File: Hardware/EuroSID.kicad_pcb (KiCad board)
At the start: 2 copper layers, 213.3 x 106.6 mm, 77 parts, among them U1 TLC5947DAP, U10 LM1117-5.0, U11 L7809, U12 STM32F030R8Tx, U13 LM1117-3.3, U2 MCP6002-xSN, U3 MCP6004, U4 OPA1678, U5 MCP6002-xSN, U6 74HC595, U7 74HC595, U8 SID, U9 LM1117-3.3

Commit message: Fixed issues with footprints
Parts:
- added D28: LM4040DBZ-10, Package_TO_SOT_SMD:SOT-23, F.Cu at (197.0, 56.0)
- added J16: Conn_ARM_JTAG_SWD_10, Connector_PinHeader_1.27mm:PinHeader_2x05_P1.27mm_Vertical_SMD, F.Cu at (199.6, 46.9)
- added Q1: MMBT3904, Package_TO_SOT_SMD:SOT-23, F.Cu at (169.4, 61.8)
- added Q2: MMBT3904, Package_TO_SOT_SMD:SOT-23, F.Cu at (172.8, 61.8)
- added Q3: MMBT3904, Package_TO_SOT_SMD:SOT-23, F.Cu at (176.3, 61.8)
- added X1: ACO-xxxMHz, Oscillator:Oscillator_DIP-14, F.Cu at (170.6, 53.6)
- C1, C10, C11, C12, C13, C14, C15, C16, C17, C18, C19, C2, C20, C21, C22, C23, C24, C25, C26, C27, C28, C3, C31, C39, C4, C40, C41, C44, C45, C48, C49, C5, C50, C51, C53, C54, C55, C56, C57, C6, C61, C62, C63, C7, C8, C9: footprint Capacitors_SMD:C_0603 -> Capacitor_SMD:C_0603_1608Metric
- moved C31 298.4 mm to (133.5, 56.2)
- moved C41 298.4 mm to (133.5, 80.0)
- moved U10 298.4 mm to (116.8, 72.6)
- moved U11 298.4 mm to (118.9, 58.9)
- moved C1 281.2 mm to (87.3, 60.3)
- moved C2 281.2 mm to (84.4, 58.9)
- moved C3 281.2 mm to (87.3, 58.9)
- moved C30 281.2 mm to (68.6, 74.1)
- moved C32 281.2 mm to (53.3, 52.0)
- moved C4 281.2 mm to (84.4, 60.3)
- moved C45 281.2 mm to (84.4, 61.6)
- moved C49 281.2 mm to (94.5, 51.6)
- moved C51 281.2 mm to (94.5, 50.3)
- moved C52 281.2 mm to (96.9, 42.0)
- moved C53 281.2 mm to (91.7, 53.9)
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
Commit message: Added PJ398SM model
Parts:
- added C65: 100 nF, Capacitor_SMD:C_0603_1608Metric, F.Cu at (165.0, 100.4)
- added C66: 100 nF, Capacitor_SMD:C_0603_1608Metric, F.Cu at (212.2, 70.6)
- added C67: 100 nF, Capacitor_SMD:C_0603_1608Metric, F.Cu at (202.2, 87.0)
- added C68: 100 nF, Capacitor_SMD:C_0603_1608Metric, F.Cu at (199.2, 90.0)
- added J1: GATE_2, Connector_Audio:Jack_3.5mm_QingPu_WQP-PJ398SM_Vertical_CircularHoles, F.Cu at (242.0, 71.5)
- added J10: IN_2, Connector_Audio:Jack_3.5mm_QingPu_WQP-PJ398SM_Vertical_CircularHoles, F.Cu at (172.6, 86.3)
- added J11: IN_3, Connector_Audio:Jack_3.5mm_QingPu_WQP-PJ398SM_Vertical_CircularHoles, F.Cu at (182.6, 71.5)
- added J12: PWM_CV, Connector_Audio:Jack_3.5mm_QingPu_WQP-PJ398SM_Vertical_CircularHoles, F.Cu at (172.6, 71.5)
- added J2: GATE_3, Connector_Audio:Jack_3.5mm_QingPu_WQP-PJ398SM_Vertical_CircularHoles, F.Cu at (231.9, 71.5)
- added J3: GATE_1, Connector_Audio:Jack_3.5mm_QingPu_WQP-PJ398SM_Vertical_CircularHoles, F.Cu at (221.0, 67.3)
- added J4: OUT2_CON, Connector_Audio:Jack_3.5mm_QingPu_WQP-PJ398SM_Vertical_CircularHoles, F.Cu at (162.5, 86.3)
- added J5: EXT_CON, Connector_Audio:Jack_3.5mm_QingPu_WQP-PJ398SM_Vertical_CircularHoles, F.Cu at (162.5, 71.5)
- added J6: CUTOFF_CV, Connector_Audio:Jack_3.5mm_QingPu_WQP-PJ398SM_Vertical_CircularHoles, F.Cu at (192.7, 86.3)
- added J7: SHAPE_CV, Connector_Audio:Jack_3.5mm_QingPu_WQP-PJ398SM_Vertical_CircularHoles, F.Cu at (202.7, 71.5)
- added J8: OUT1_CON, Connector_Audio:Jack_3.5mm_QingPu_WQP-PJ398SM_Vertical_CircularHoles, F.Cu at (192.7, 71.5)
- added J9: IN_1, Connector_Audio:Jack_3.5mm_QingPu_WQP-PJ398SM_Vertical_CircularHoles, F.Cu at (182.6, 86.3)
- added R1: 1640, Resistor_SMD:R_0603_1608Metric, F.Cu at (224.4, 85.5)
- added R10: 100k, Resistor_SMD:R_0603_1608Metric, F.Cu at (248.5, 75.1)
- added R11: 10k, Resistor_SMD:R_0603_1608Metric, F.Cu at (239.4, 85.5)
- added R12: 10k, Resistor_SMD:R_0603_1608Metric, F.Cu at (236.4, 87.0)
- added R13: 10k, Resistor_SMD:R_0603_1608Metric, F.Cu at (248.5, 73.6)
- added R14: 10k, Resistor_SMD:R_0603_1608Metric, F.Cu at (233.4, 87.0)
- added R15: 10k, Resistor_SMD:R_0603_1608Metric, F.Cu at (236.4, 85.5)
- added R16: 10k, Resistor_SMD:R_0603_1608Metric, F.Cu at (233.4, 85.5)
- added R17: 10k, Resistor_SMD:R_0603_1608Metric, F.Cu at (230.4, 87.0)
- added R18: 10k, Resistor_SMD:R_0603_1608Metric, F.Cu at (248.5, 78.2)
- added R19: 10k, Resistor_SMD:R_0603_1608Metric, F.Cu at (218.4, 85.5)
- added R2: 10k, Resistor_SMD:R_0603_1608Metric, F.Cu at (218.4, 87.0)
- added R20: 10k, Resistor_SMD:R_0603_1608Metric, F.Cu at (230.4, 85.5)
- added R21: 10k, Resistor_SMD:R_0603_1608Metric, F.Cu at (248.5, 72.1)
- added R22: 10k, Resistor_SMD:R_0603_1608Metric, F.Cu at (227.4, 85.5)
- added R23: 10k, Resistor_SMD:R_0603_1608Metric, F.Cu at (224.4, 87.0)
- added R24: 10k, Resistor_SMD:R_0603_1608Metric, F.Cu at (168.0, 100.4)
- added R25: 30k, Resistor_SMD:R_0603_1608Metric, F.Cu at (171.0, 100.4)
- added R26: 1k, Resistor_SMD:R_0603_1608Metric, F.Cu at (174.0, 100.4)
- added R27: 50k, Resistor_SMD:R_0603_1608Metric, F.Cu at (199.2, 85.5)
- added R28: 10k, Resistor_SMD:R_0603_1608Metric, F.Cu at (177.0, 100.4)
- added R29: 30k, Resistor_SMD:R_0603_1608Metric, F.Cu at (209.2, 70.6)
- added R3: 10k, Resistor_SMD:R_0603_1608Metric, F.Cu at (221.4, 85.5)
- added R30: 120k, Resistor_SMD:R_0603_1608Metric, F.Cu at (180.1, 100.4)
- added R31: 100k, Resistor_SMD:R_0603_1608Metric, F.Cu at (162.0, 100.4)
- added R32: 120k, Resistor_SMD:R_0603_1608Metric, F.Cu at (159.0, 100.4)
- added R33: 100k, Resistor_SMD:R_0603_1608Metric, F.Cu at (209.2, 72.1)
- added R34: 120k, Resistor_SMD:R_0603_1608Metric, F.Cu at (202.2, 85.5)
- added R35: 120k, Resistor_SMD:R_0603_1608Metric, F.Cu at (212.2, 72.1)
- added R36: 1k, Resistor_SMD:R_0603_1608Metric, F.Cu at (209.2, 73.6)
- added R37: 180k, Resistor_SMD:R_0603_1608Metric, F.Cu at (209.2, 75.1)
- added R38: 100k, Resistor_SMD:R_0603_1608Metric, F.Cu at (183.1, 100.4)
- added R39: 180k, Resistor_SMD:R_0603_1608Metric, F.Cu at (199.2, 87.0)
- added R4: 10k, Resistor_SMD:R_0603_1608Metric, F.Cu at (248.5, 70.6)
- added R40: 100k, Resistor_SMD:R_0603_1608Metric, F.Cu at (209.2, 76.6)
- added R41: 180k, Resistor_SMD:R_0603_1608Metric, F.Cu at (212.2, 73.6)
- added R42: 100k, Resistor_SMD:R_0603_1608Metric, F.Cu at (212.2, 75.1)
- added R43: 120k, Resistor_SMD:R_0603_1608Metric, F.Cu at (212.2, 76.6)
- added R44: 100k, Resistor_SMD:R_0603_1608Metric, F.Cu at (209.2, 78.2)
- added R45: 47k, Resistor_SMD:R_0603_1608Metric, F.Cu at (199.2, 88.5)
- added R46: 47k, Resistor_SMD:R_0603_1608Metric, F.Cu at (186.1, 100.4)
- added R47: 120k, Resistor_SMD:R_0603_1608Metric, F.Cu at (205.2, 85.5)
- added R48: 120k, Resistor_SMD:R_0603_1608Metric, F.Cu at (189.1, 100.4)
- added R49: 1K, Resistor_SMD:R_0603_1608Metric, F.Cu at (218.4, 93.0)
- added R5: 10k, Resistor_SMD:R_0603_1608Metric, F.Cu at (221.4, 87.0)
- added R50: 1k, Resistor_SMD:R_0603_1608Metric, F.Cu at (159.0, 106.8)
- added R51: 1k, Resistor_SMD:R_0603_1608Metric, F.Cu at (159.0, 105.3)
- added R6: 10k, Resistor_SMD:R_0603_1608Metric, F.Cu at (227.4, 87.0)
- added R7: 10k, Resistor_SMD:R_0603_1608Metric, F.Cu at (242.4, 85.5)
- added R8: 100k, Resistor_SMD:R_0603_1608Metric, F.Cu at (248.5, 76.6)
- added R9: 100k, Resistor_SMD:R_0603_1608Metric, F.Cu at (239.4, 87.0)
- C29, C30, C58: footprint Capacitors_Tantalum_SMD:CP_Tantalum_Case-R_EIA-2012-12_Reflow -> Capacitor_Tantalum_SMD:CP_EIA-2012-12_Kemet-R
- C32: footprint Capacitors_SMD:CP_Elec_10x10 -> Capacitor_SMD:CP_Elec_10x10
- C33, C34, C35, C36, C37, C38, C42, C43, C46, C47: footprint Capacitors_SMD:CP_Elec_4x5.3 -> Capacitor_SMD:CP_Elec_4x5.3
- C52, C60, C64: footprint Capacitors_Tantalum_SMD:CP_Tantalum_Case-A_EIA-3216-18_Reflow -> Capacitor_Tantalum_SMD:CP_EIA-3216-18_Kemet-A
- C59: footprint Capacitors_SMD:CP_Elec_4x5.7 -> Capacitor_SMD:CP_Elec_4x5.7
- J16: footprint Connector_PinHeader_1.27mm:PinHeader_2x05_P1.27mm_Vertical_SMD -> Connector_PinHeader_1.27mm:PinHeader_2x05_P1.27mm_Vertical
- U1: footprint Housings_SSOP:HTSSOP-32_6.1x11mm_Pitch0.65mm_ThermalPad -> Package_SO:HTSSOP-32-1EP_6.1x11mm_P0.65mm_EP5.2x11mm_Mask4.11x4.36mm_ThermalVias
- U10, U13, U9: footprint TO_SOT_Packages_SMD:SOT-223-3_TabPin2 -> Package_TO_SOT_SMD:SOT-223-3_TabPin2
- U11: footprint TO_SOT_Packages_SMD:TO-252-3_TabPin2 -> Package_TO_SOT_SMD:TO-252-3_TabPin2
- U12: footprint Housings_QFP:HTQFP-64-1EP_10x10mm_Pitch0.5mm_ThermalPad -> Package_QFP:LQFP-64_10x10mm_P0.5mm
- U2, U4, U5: footprint Housings_SOIC:SOIC-8_3.9x4.9mm_Pitch1.27mm -> Package_SO:SOIC-8_3.9x4.9mm_P1.27mm
- U3: footprint Housings_SSOP:TSSOP-14_4.4x5mm_Pitch0.65mm -> Package_SO:TSSOP-14_4.4x5mm_P0.65mm
- U6, U7: footprint Housings_SOIC:SOIC-16_3.9x9.9mm_Pitch1.27mm -> Package_SO:SOIC-16_3.9x9.9mm_P1.27mm
- U8: footprint Housings_DIP:DIP-28_W15.24mm_Socket -> Package_DIP:DIP-28_W15.24mm_Socket
- moved C46 186.2 mm to (63.5, 133.3)
- moved C40 172.5 mm to (73.2, 109.2)
- moved U1 158.4 mm to (64.8, 119.4)
- moved U13 148.6 mm to (80.8, 118.4)
- moved U9 148.6 mm to (94.8, 117.1)
- moved C33 136.6 mm to (109.2, 102.9)
- moved C37 135.8 mm to (108.5, 83.8)
- moved Q3 123.4 mm to (60.7, 105.0)
- moved Q1 123.4 mm to (53.8, 105.0)
- moved X1 123.4 mm to (55.1, 96.8)
- moved Q2 123.4 mm to (57.2, 105.0)
- moved U7 113.7 mm to (70.2, 48.8)
- moved C29 113.7 mm to (68.9, 55.4)
- moved C12 100.7 mm to (92.2, 131.8)
- moved C15 100.7 mm to (101.5, 126.2)
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
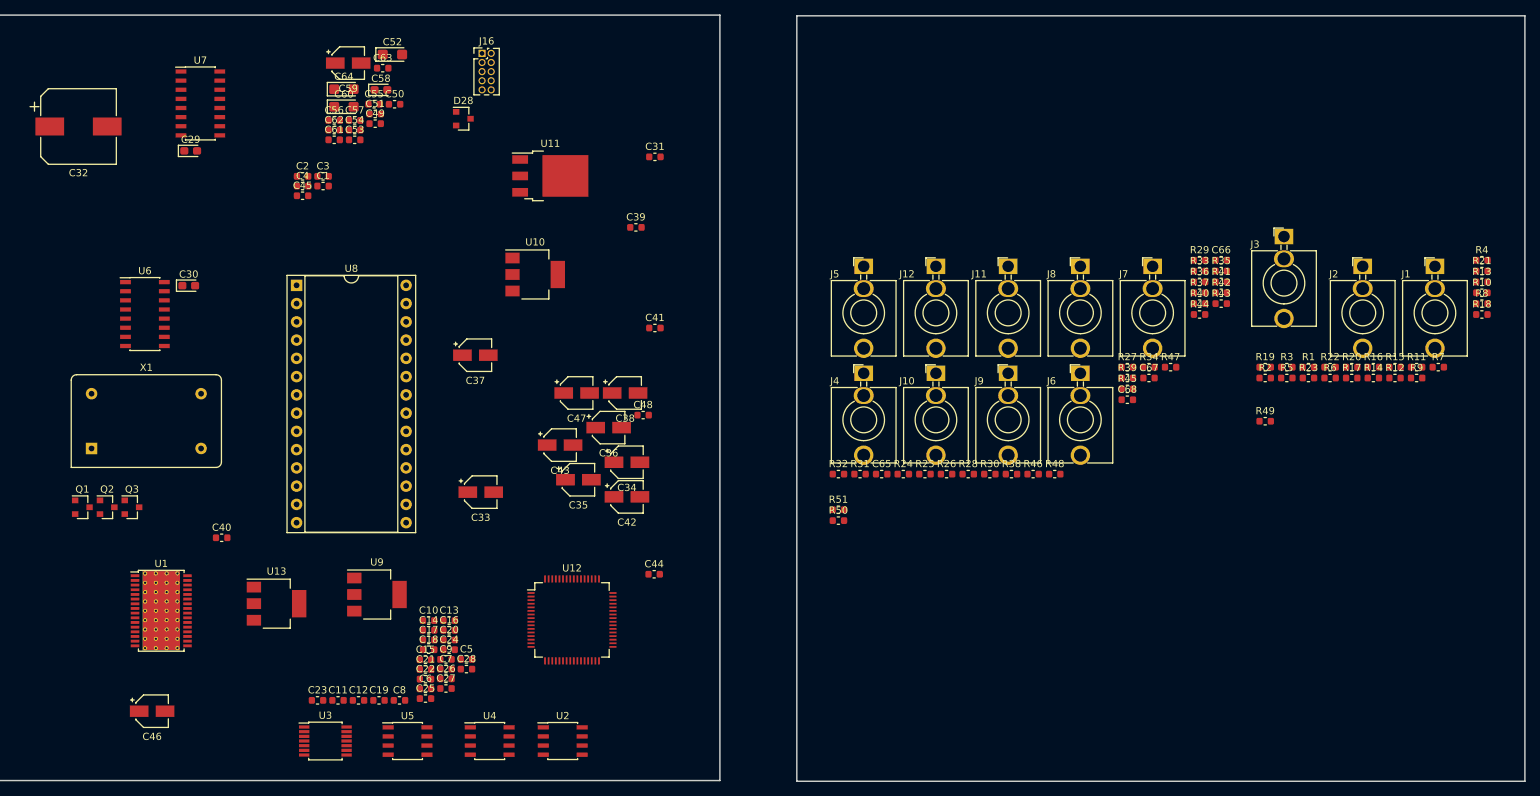
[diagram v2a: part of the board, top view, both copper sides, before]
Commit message: Finished assigning footprints
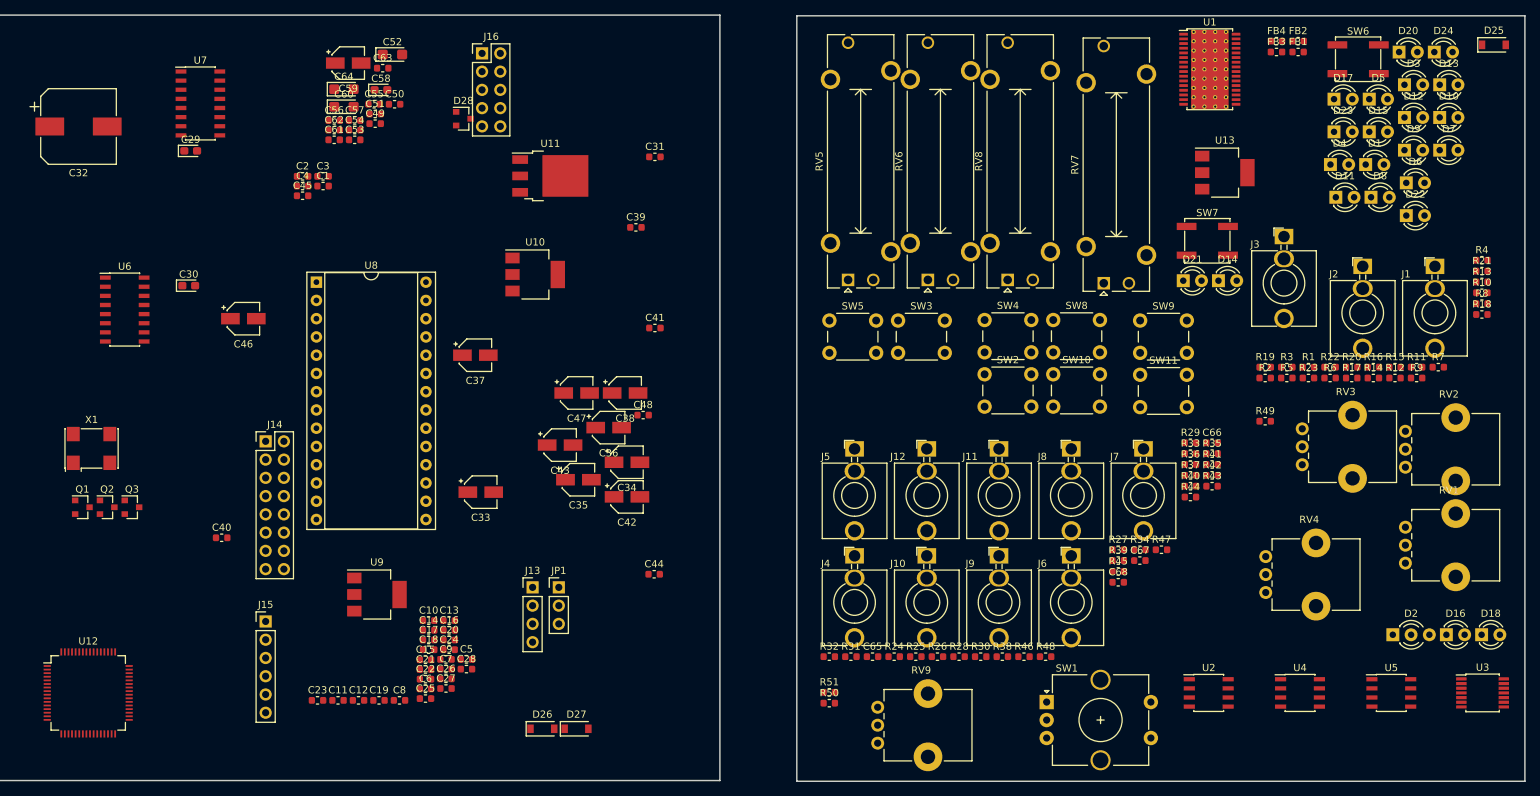
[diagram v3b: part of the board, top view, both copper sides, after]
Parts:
- added D1: VOICE1, LED_THT:LED_D3.0mm, F.Cu at (232.3, 57.3)
- added D10: BP, LED_THT:LED_D3.0mm, F.Cu at (242.6, 50.7)
- added D11: TRIANGLE, LED_THT:LED_D3.0mm, F.Cu at (228.2, 61.8)
- added D12: DECAY, LED_THT:LED_D3.0mm, F.Cu at (237.7, 50.7)
- added D13: VOICE3, LED_THT:LED_D3.0mm, F.Cu at (242.6, 46.2)
- added D14: SID2, LED_THT:LED_D3.0mm, F.Cu at (211.9, 73.5)
- added D15: FILTEREXT, LED_THT:LED_D3.0mm, F.Cu at (232.8, 52.7)
- added D16: MOD, LED_THT:LED_D3.0mm, F.Cu at (243.6, 122.7)
- added D17: SAW, LED_THT:LED_D3.0mm, F.Cu at (227.9, 48.2)
- added D18: SUSTAIN, LED_THT:LED_D3.0mm, F.Cu at (248.5, 122.7)
- added D2: MODE_RG, LED_THT:LED_D3.0mm-3, F.Cu at (236.1, 122.7)
- added D20: FILTER1, LED_THT:LED_D3.0mm, F.Cu at (237.0, 41.6)
- added D21: LP, LED_THT:LED_D3.0mm, F.Cu at (207.0, 73.5)
- added D22: SYNC, LED_THT:LED_D3.0mm, F.Cu at (238.0, 64.4)
- added D23: SYNC, LED_THT:LED_D3.0mm, F.Cu at (227.9, 52.7)
- added D24: RELEASE, LED_THT:LED_D3.0mm, F.Cu at (241.9, 41.6)
- added D25: BZT52-C5V1J, Diode_SMD:D_SOD-123, F.Cu at (250.2, 40.6)
- added D26: 1N5819HW-7-F, Diode_SMD:D_SOD-123, F.Cu at (117.8, 135.8)
- added D27: 1N5819HW-7-F, Diode_SMD:D_SOD-123, F.Cu at (122.5, 135.8)
- added D3: FILTER2, LED_THT:LED_D3.0mm, F.Cu at (237.7, 46.2)
- added D4: HP, LED_THT:LED_D3.0mm, F.Cu at (227.4, 57.3)
- added D5: SQUARE, LED_THT:LED_D3.0mm, F.Cu at (232.8, 48.2)
- added D6: ATTACK, LED_THT:LED_D3.0mm, F.Cu at (238.0, 59.8)
- added D7: VOICE2, LED_THT:LED_D3.0mm, F.Cu at (242.6, 55.3)
- added D8: SID1, LED_THT:LED_D3.0mm, F.Cu at (233.1, 61.8)
- added D9: FILTER3, LED_THT:LED_D3.0mm, F.Cu at (237.7, 55.3)
- added FB1: Ferrite_Bead, Inductor_SMD:L_0603_1608Metric, F.Cu at (222.9, 41.6)
- added FB2: Ferrite_Bead, Inductor_SMD:L_0603_1608Metric, F.Cu at (222.9, 40.1)
- added FB3: Ferrite_Bead, Inductor_SMD:L_0603_1608Metric, F.Cu at (219.9, 41.6)
- added FB4: Ferrite_Bead, Inductor_SMD:L_0603_1608Metric, F.Cu at (219.9, 40.1)
- added J13: Conn_01x04_Female, Connector_PinHeader_2.54mm:PinHeader_1x04_P2.54mm_Vertical, F.Cu at (116.4, 116.1)
- added J14: Eurorack Connector, Connector_PinHeader_2.54mm:PinHeader_2x08_P2.54mm_Vertical, F.Cu at (79.3, 95.8)
- added J15: Conn_01x06_Male, Connector_PinHeader_2.54mm:PinHeader_1x06_P2.54mm_Vertical, F.Cu at (79.3, 120.9)
- added JP1: Jumper_3_Bridged12, Connector_PinHeader_2.54mm:PinHeader_1x03_P2.54mm_Vertical, F.Cu at (120.1, 116.1)
- added RV1: RESONANCE, Potentiometer_THT:Potentiometer_Bourns_PTV09A-1_Single_Vertical, F.Cu at (237.9, 112.8)
- added RV2: PWM, Potentiometer_THT:Potentiometer_Bourns_PTV09A-1_Single_Vertical, F.Cu at (237.9, 99.4)
- added RV3: FREQ-ATTEN, Potentiometer_THT:Potentiometer_Bourns_PTV09A-1_Single_Vertical, F.Cu at (223.5, 99.1)
- added RV4: CUTOFF, Potentiometer_THT:Potentiometer_Bourns_PTV09A-1_Single_Vertical, F.Cu at (218.4, 116.8)
- added RV5: ATTACK, Potentiometer_THT:Potentiometer_Bourns_PTA2043_Single_Slide, F.Cu at (160.3, 73.3)
- added RV6: DECAY, Potentiometer_THT:Potentiometer_Bourns_PTA2043_Single_Slide, F.Cu at (171.4, 73.3)
- added RV7: SUSTAIN, Potentiometer_THT:Potentiometer_Bourns_PTA2043_Single_Slide, F.Cu at (195.9, 73.8)
- added RV8: RELEASE, Potentiometer_THT:Potentiometer_Bourns_PTA2043_Single_Slide, F.Cu at (182.5, 73.3)
- added RV9: 50k, Potentiometer_THT:Potentiometer_Bourns_PTV09A-1_Single_Vertical, F.Cu at (164.4, 137.8)
- added SW1: Frequency Adjust, Rotary_Encoder:RotaryEncoder_Alps_EC12E-Switch_Vertical_H20mm_CircularMountingHoles, F.Cu at (188.0, 132.1)
- added SW10: FILTER_SW, Button_Switch_THT:SW_PUSH_6mm_H9.5mm, F.Cu at (188.9, 86.5)
- added SW11: FILTEREXT_SW, Button_Switch_THT:SW_PUSH_6mm_H9.5mm, F.Cu at (201.0, 86.5)
- added SW2: MOD_SW, Button_Switch_THT:SW_PUSH_6mm_H9.5mm, F.Cu at (179.3, 86.5)
- added SW3: FILTER1_SW, Button_Switch_THT:SW_PUSH_6mm_H9.5mm, F.Cu at (167.3, 79.0)
- added SW4: VOICE_SW, Button_Switch_THT:SW_PUSH_6mm_H9.5mm, F.Cu at (179.3, 78.9)
- added SW5: FILTER2_SW, Button_Switch_THT:SW_PUSH_6mm_H9.5mm, F.Cu at (157.7, 79.0)
- added SW6: PROG, Button_Switch_SMD:SW_SPST_EVPBF, F.Cu at (231.3, 42.6)
- added SW7: RST, Button_Switch_SMD:SW_SPST_EVPBF, F.Cu at (210.3, 67.9)
- added SW8: MODE_SW, Button_Switch_THT:SW_PUSH_6mm_H9.5mm, F.Cu at (188.9, 78.9)
- added SW9: FILTER3_SW, Button_Switch_THT:SW_PUSH_6mm_H9.5mm, F.Cu at (201.0, 79.0)
- J16: footprint Connector_PinHeader_1.27mm:PinHeader_2x05_P1.27mm_Vertical -> Connector_PinHeader_2.54mm:PinHeader_2x05_P2.54mm_Vertical
- R49: value 1K -> 1k
- X1: value ACO-xxxMHz -> ECS-8FMX-010-TR; footprint Oscillator:Oscillator_DIP-14 -> Oscillator:Oscillator_SMD_Abracon_ASV-4Pin_7.0x5.1mm
- moved U1 164.2 mm to (210.7, 44.0)
- moved U3 161.1 mm to (248.6, 130.8)
- moved U13 144.9 mm to (212.8, 58.4)
- moved U5 137.0 mm to (235.9, 130.8)
- moved U4 112.9 mm to (223.2, 130.8)
- moved U2 90.1 mm to (210.5, 130.8)
- moved U12 68.1 mm to (54.6, 130.8)
- moved C46 56.1 mm to (76.2, 78.7)
- moved C68 25.4 mm to (197.9, 115.4)
- moved J11 25.4 mm to (181.3, 96.9)
- moved J12 25.4 mm to (171.3, 96.9)
- moved J5 25.4 mm to (161.2, 96.9)
- moved J7 25.4 mm to (201.4, 96.9)
- moved J8 25.4 mm to (191.4, 96.9)
- moved R27 25.4 mm to (197.9, 110.9)
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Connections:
- X1 pad 1: Net-(X1-Pad1) -> +5V
